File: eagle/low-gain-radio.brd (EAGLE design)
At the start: 99 x 98 mm, 131 parts, among them U1 MKW01Z128, U2 SKY65116, U3 W25Q80DV, U4 LP5907MFX-3.3, U6 LP5907MFX-3.3, U7 LD39200, U8 MAAL-010704, Y1 32MHz

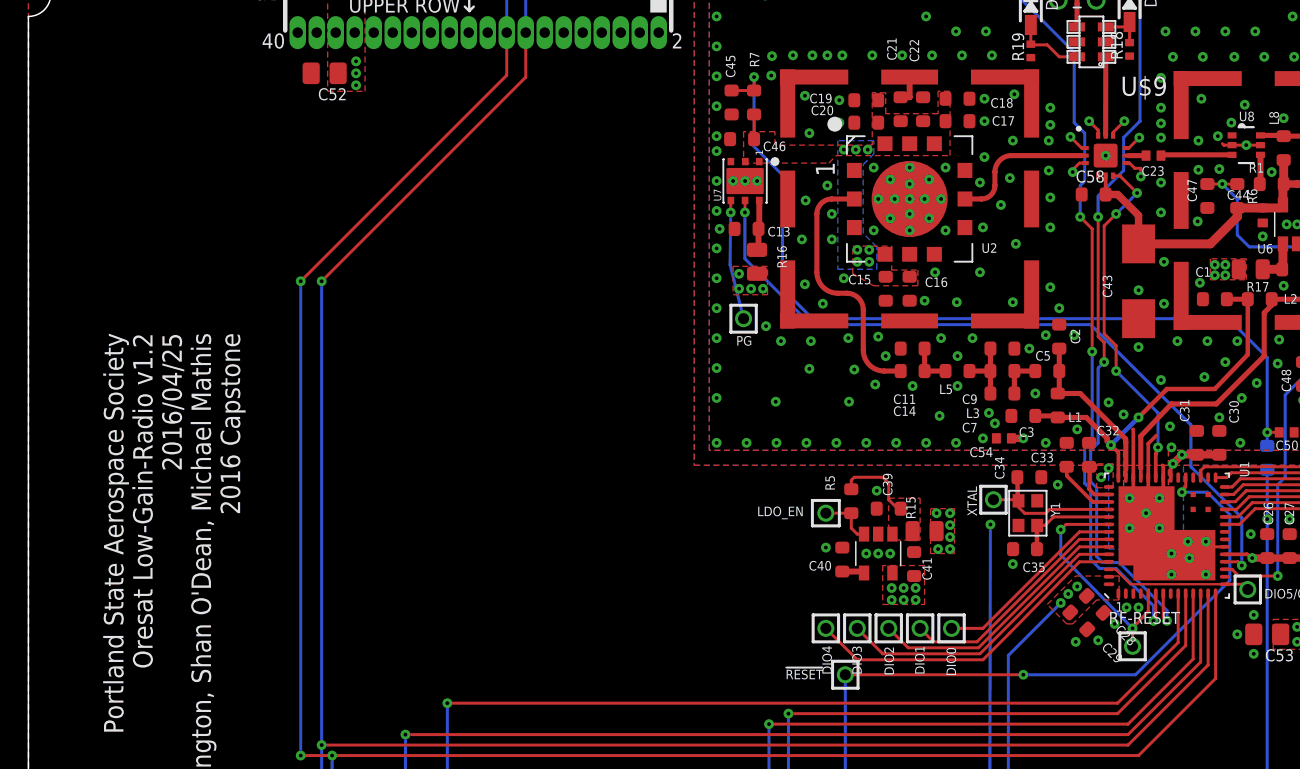
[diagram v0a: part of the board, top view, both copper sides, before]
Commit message: small tweaks on layout, including more gnd vias
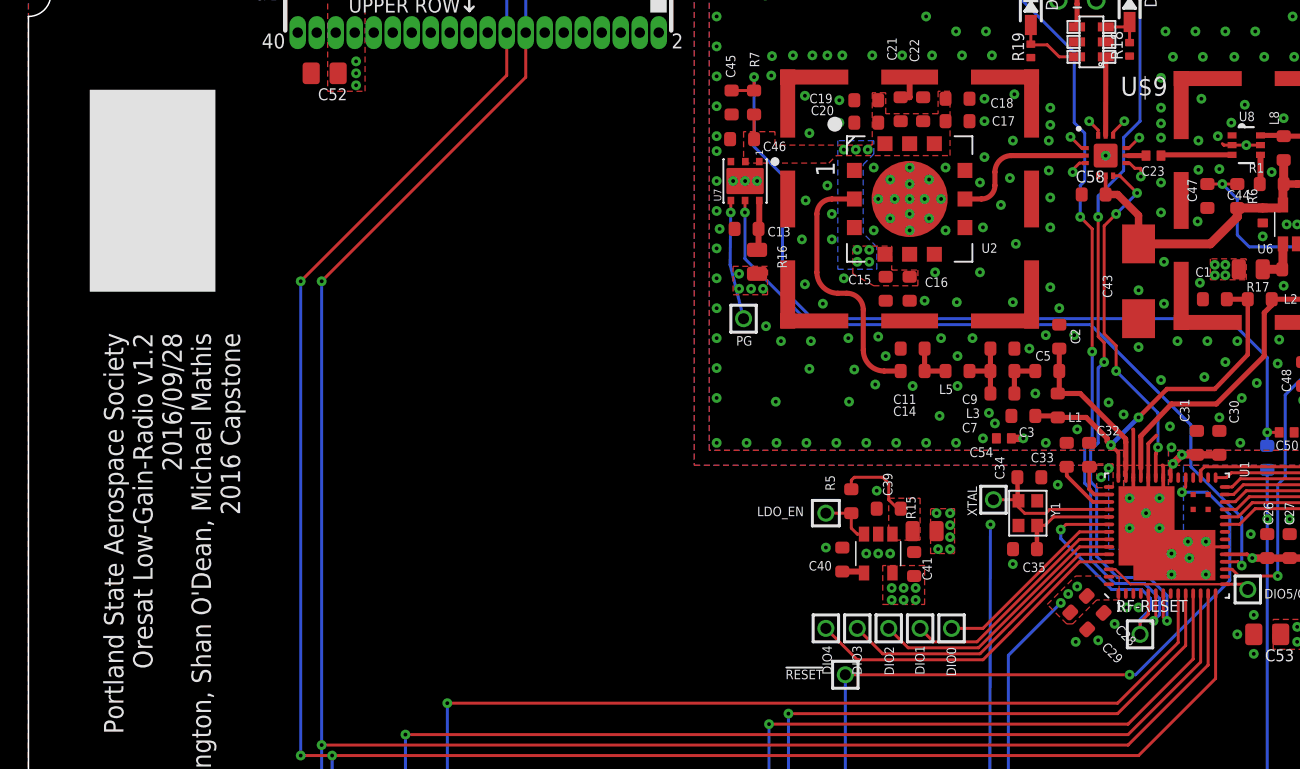
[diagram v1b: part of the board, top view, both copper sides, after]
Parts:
- moved RF-RESET 0.94 mm to (74.3, 48.7)
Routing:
- net RF_RESET: track 15.9 -> 17.3 mm, vias 2 -> 1
- net VFWD: track 51.9 -> 52.7 mm
- net VREV: track 51.6 -> 52.2 mm
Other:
- board text added: "Portland State Aerospace Society Oresat Low-Gain-Radio v1.2 2016/09/28 James Heath, Will Harrington, Shan O'Dean, Michael Mathis 2016 Capstone"
- board text removed: "Portland State Aerospace Society Oresat Low-Gain-Radio v1.2 2016/04/25 James Heath, Will Harrington, Shan O'Dean, Michael Mathis 2016 Capstone"
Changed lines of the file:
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@@
 <text x="5.05" y="68.85" size="1.3" layer="21" font="vector" ratio="15" rot="R270">Portland State Aerospace Society
 Oresat Low-Gain-Radio v1.2
-2016/04/25
+2016/09/28
 James Heath, Will Harrington, Shan O'Dean, Michael Mathis
 2016 Capstone</text>
@@
 <wire x1="56.3" y1="78.2" x2="56.3" y2="77.3" width="0.1" layer="41"/>
 <wire x1="58.5" y1="80.35" x2="59.3" y2="80.35" width="0.01" layer="41"/>
+<rectangle x1="4.1" y1="71.6" x2="12.5" y2="85.1" layer="21"/>
 </plain>
 <attributes>
@@
 <element name="CF2" library="oresat-eagle" package="CON-MMCX-F-MOLEX-0734151001" value="CON-MMCX-F-MOLEX-0734151001" x="70.1" y="92.35"/>
 <element name="U$35" library="oresat-eagle" package="ORESAT-CARD-RF-V0.4" value="" x="0" y="0"/>
-<element name="RF-RESET" library="Tova" package="2MM-TEST-POINT" value="TEST-POINT" x="73.8" y="47.9"/>
+<element name="RF-RESET" library="Tova" package="2MM-TEST-POINT" value="TEST-POINT" x="74.3" y="48.7"/>
 <element name="C58" library="rcl_custom" package=".0603-B-NOSILK" value="10nF" x="71.2" y="78.1">
 <attribute name="DIST" value="Digi-Key" x="71.2" y="78.1" size="1.778" layer="27" display="off"/>
@@
 <contactref element="CM1" pad="10"/>
 <contactref element="U1" pad="33"/>
-<via x="66.5" y="46" extent="1-16" drill="0.254"/>
+<via x="73.6" y="46" extent="1-16" drill="0.254"/>
 <contactref element="!RESET" pad="1"/>
 <wire x1="77.35" y1="59.1778" x2="77.35" y2="58.55" width="0.2" layer="1"/>
@@
 <wire x1="78.8" y1="58.2" x2="80.3" y2="56.7" width="0.2" layer="16"/>
 <wire x1="80.3" y1="56.7" x2="80.3" y2="52.3" width="0.2" layer="16"/>
-<wire x1="66.5" y1="46" x2="54.6" y2="46" width="0.2" layer="1"/>
+<wire x1="73.6" y1="46" x2="54.6" y2="46" width="0.2" layer="1"/>
 <wire x1="54.6" y1="46" x2="54.6" y2="4.055" width="0.2" layer="16"/>
 <wire x1="54.6" y1="4.055" x2="54.61" y2="4.045" width="0.2" layer="16"/>
 <wire x1="80.3" y1="52.3" x2="74" y2="46" width="0.2" layer="16"/>
-<wire x1="74" y1="46" x2="66.5" y2="46" width="0.2" layer="16"/>
+<wire x1="74" y1="46" x2="73.6" y2="46" width="0.2" layer="16"/>
 </signal>
 <signal name="N$4">
@@
 <wire x1="75.85" y1="49.85" x2="76.1" y2="49.6" width="0.2" layer="1"/>
 <via x="76.1" y="49.6" extent="1-16" drill="0.254"/>
-<wire x1="76.1" y1="49.6" x2="76.1" y2="50.3" width="0.2" layer="16"/>
-<wire x1="76.1" y1="50.3" x2="72.9" y2="53.5" width="0.2" layer="16"/>
-<wire x1="72.9" y1="53.5" x2="71.8" y2="53.5" width="0.2" layer="16"/>
-<wire x1="71.8" y1="53.5" x2="71.4" y2="53.9" width="0.2" layer="16"/>
 <wire x1="71.4" y1="53.9" x2="71.4" y2="58.5" width="0.2" layer="16"/>
 <via x="71.9" y="66.9" extent="1-16" drill="0.254"/>
@@
 <wire x1="75.45" y1="93.5" x2="76.25" y2="93.5" width="0.2" layer="1"/>
 <wire x1="76.25" y1="93.5" x2="76.3" y2="93.45" width="0.2" layer="1"/>
+<wire x1="71.4" y1="53.9" x2="72.8" y2="52.5" width="0.2" layer="16"/>
+<wire x1="72.8" y1="52.5" x2="74.9" y2="52.5" width="0.2" layer="16"/>
+<wire x1="74.9" y1="52.5" x2="76.1" y2="51.3" width="0.2" layer="16"/>
+<wire x1="76.1" y1="51.3" x2="76.1" y2="49.6" width="0.2" layer="16"/>
 </signal>
 <signal name="FWD">
@@
 <wire x1="75.35" y1="49.75" x2="75.2" y2="49.6" width="0.2" layer="1"/>
 <via x="75.2" y="49.6" extent="1-16" drill="0.254"/>
-<wire x1="75.2" y1="49.6" x2="75.2" y2="50.6" width="0.2" layer="16"/>
-<wire x1="75.2" y1="50.6" x2="72.7" y2="53.1" width="0.2" layer="16"/>
-<wire x1="72.7" y1="53.1" x2="71.6" y2="53.1" width="0.2" layer="16"/>
-<wire x1="71.6" y1="53.1" x2="71" y2="53.7" width="0.2" layer="16"/>
 <wire x1="71" y1="53.7" x2="71" y2="58.4" width="0.2" layer="16"/>
 <via x="71.1" y="67.6" extent="1-16" drill="0.254"/>
@@
 <wire x1="65.25" y1="93.3" x2="64.45" y2="93.3" width="0.2" layer="1"/>
 <wire x1="64.45" y1="93.3" x2="64.4" y2="93.25" width="0.2" layer="1"/>
+<wire x1="71" y1="53.7" x2="72.6" y2="52.1" width="0.2" layer="16"/>
+<wire x1="72.6" y1="52.1" x2="74.6" y2="52.1" width="0.2" layer="16"/>
+<wire x1="74.6" y1="52.1" x2="75.6" y2="51.1" width="0.2" layer="16"/>
+<wire x1="75.2" y1="49.6" x2="75.6" y2="50" width="0.2" layer="16"/>
+<wire x1="75.6" y1="50" x2="75.6" y2="51.1" width="0.2" layer="16"/>
 </signal>
 <signal name="RF_RESET">
 <contactref element="U1" pad="5"/>
 <contactref element="U1" pad="48"/>
-<wire x1="74.85" y1="51.4222" x2="74.85" y2="50.25" width="0.2" layer="1"/>
-<wire x1="74.85" y1="50.25" x2="73.8" y2="49.1" width="0.2" layer="1"/>
-<via x="73.8" y="49.1" extent="1-16" drill="0.254"/>
-<wire x1="73.8" y1="49.1" x2="69" y2="54" width="0.2" layer="16"/>
-<wire x1="69" y1="54" x2="69" y2="55.7" width="0.2" layer="16"/>
+<wire x1="74.85" y1="51.4222" x2="74.85" y2="50.05" width="0.2" layer="1"/>
 <via x="69" y="55.7" extent="1-16" drill="0.254"/>
+<wire x1="69" y1="55.1" x2="69" y2="55.7" width="0.2" layer="16"/>
 <wire x1="69" y1="55.7" x2="69.35" y2="56.05" width="0.2" layer="1"/>
 <wire x1="72.2222" y1="56.05" x2="69.35" y2="56.05" width="0.2" layer="1"/>
 <contactref element="RF-RESET" pad="1"/>
-<wire x1="73.8" y1="47.9" x2="73.8" y2="49.1" width="0.2" layer="1"/>
+<wire x1="74.85" y1="50.05" x2="74.3" y2="49.5" width="0.2" layer="1"/>
+<wire x1="74.3" y1="49.5" x2="74.3" y2="48.7" width="0.2" layer="1"/>
+<wire x1="74.3" y1="48.7" x2="74.3" y2="49.7" width="0.2" layer="16"/>
+<wire x1="74.3" y1="49.7" x2="75" y2="50.4" width="0.2" layer="16"/>
+<wire x1="75" y1="50.4" x2="75" y2="51.1" width="0.2" layer="16"/>
+<wire x1="75" y1="51.1" x2="74.4" y2="51.7" width="0.2" layer="16"/>
+<wire x1="74.4" y1="51.7" x2="72.4" y2="51.7" width="0.2" layer="16"/>
+<wire x1="72.4" y1="51.7" x2="69" y2="55.1" width="0.2" layer="16"/>
 </signal>
 <signal name="N$12">

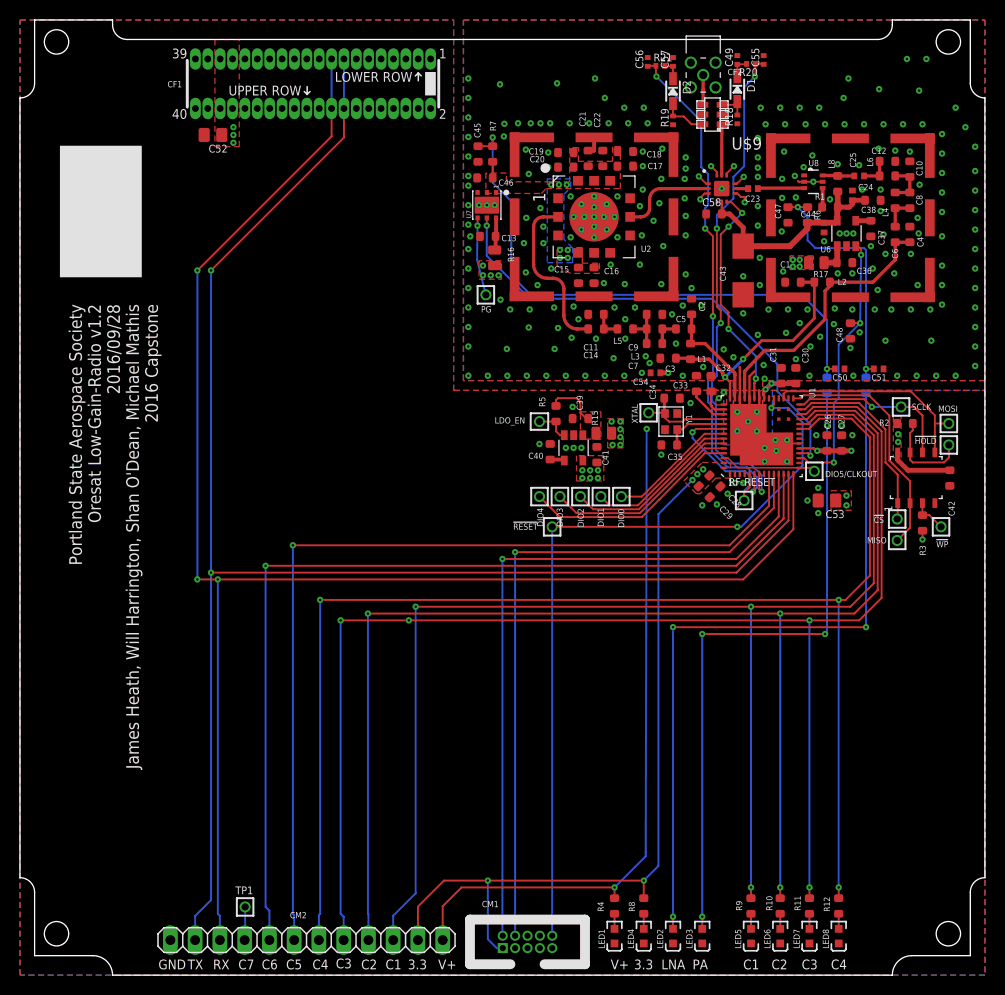
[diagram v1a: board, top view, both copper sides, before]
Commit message: added new RF switch, started layout but its unfinished, still need to hook GPIO to 40 pin connector as well
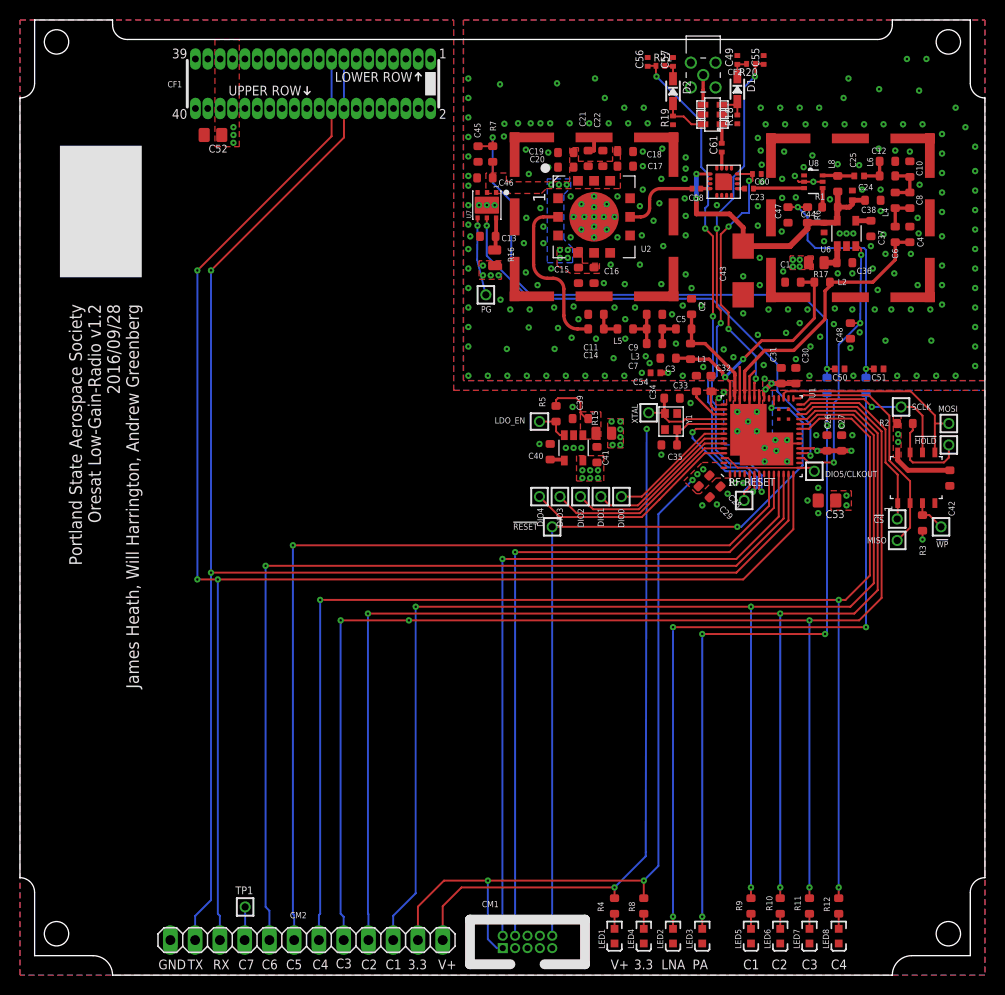
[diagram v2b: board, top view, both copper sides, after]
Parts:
- removed U$9: PE42723, low-gain-radio:PE42723
- added C60, C61: 100pF, low-gain-radio:.0402-C-NOSILK
- added U$49: RF3025, low-gain-radio:QFN-16_3MMX3MM
- C23: value 1nF -> 100pF; device rcl_custom:.0402-B-NOSILK -> low-gain-radio:.0402-C-NOSILK
- C58: value 10nF -> 100pF; device rcl_custom:.0603-B-NOSILK -> low-gain-radio:.0402-C-NOSILK
- moved C58 3.16 mm to (69.4, 80.7)
- moved C23 0.40 mm to (74.8, 80.7), turned to 180 degrees
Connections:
- new net RFOUT: C58.1, U2.8
- new net RXTX_OUT: C61.1, U$49.RFC
- net LNA_IN: now also C23.2, U$49.RF2; no longer C23.1, U$9.8
- net N$25: now also C23.1; no longer C23.2
- net PA_IN: now also C58.2, U$49.RF1; no longer U$9.2, U2.8
- net RFC: now also C61.2; no longer U$9.11
- net RF_GND: now also C60.1, U$49.GND, U$49.GND1, U$49.GND10, U$49.GND2, U$49.GND3, U$49.GND4, U$49.GND5, U$49.GND6, U$49.GND7, U$49.GND8, U$49.GND9, U$49.PADDLE; no longer C58.1, U$9.1, U$9.10, U$9.12, U$9.3, U$9.7, U$9.9
- net RXTX: now also C60.2, U$49.VC; no longer U$9.6
- net VBIAS: now also U$49.VDD; no longer C58.2, U$9.5
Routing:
- net PA_IN: track 9.78 -> 0.95 mm
- net RFOUT: track 0.00 -> 8.08 mm
- net RF_GND: track 26.1 -> 18.3 mm, vias 253 -> 247
- net VBIAS: track 23.5 -> 30.3 mm, vias 0 -> 2
- net RXTX: track 23.5 -> 28.0 mm
- net RFC: track 5.25 -> 1.96 mm
- net RXTX_OUT: track 0.00 -> 1.65 mm
- net LNA_IN: track 1.35 -> 0.75 mm
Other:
- board text added: "Portland State Aerospace Society Oresat Low-Gain-Radio v1.2 2016/09/28 James Heath, Will Harrington, Andrew Greenberg"
- board text removed: "Portland State Aerospace Society Oresat Low-Gain-Radio v1.2 2016/09/28 James Heath, Will Harrington, Shan O'Dean, Michael Mathis 2016 Capstone"

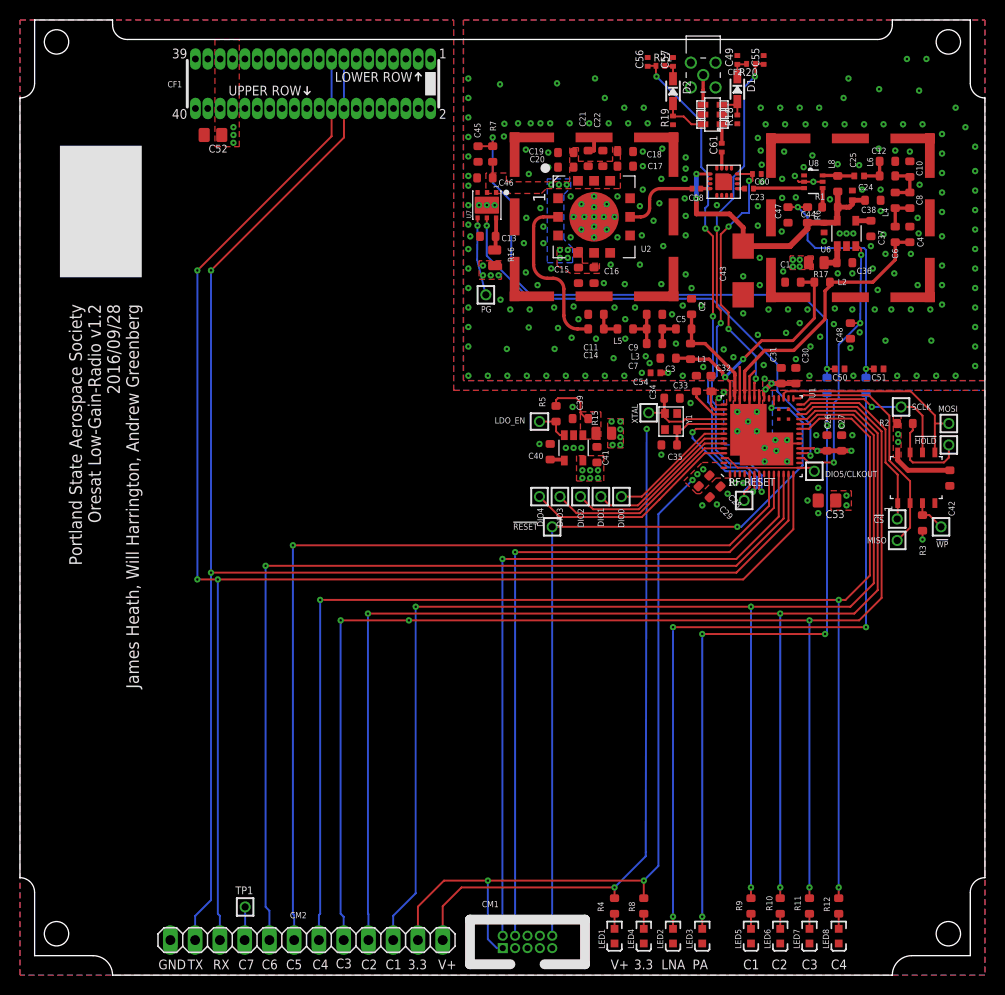
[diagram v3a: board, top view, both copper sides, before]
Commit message: finished with laying out the rf switch, placed and routed GPIO line for LLWU
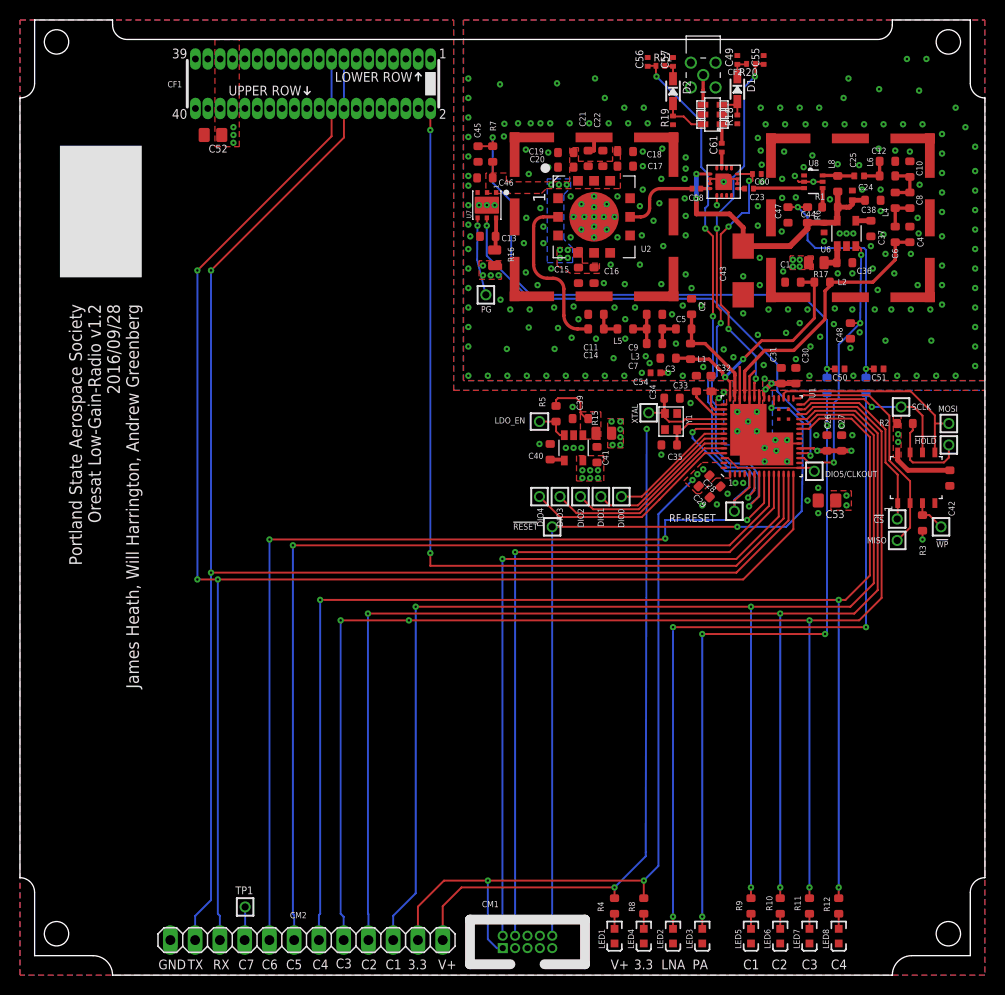
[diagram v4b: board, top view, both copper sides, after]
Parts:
- moved RF-RESET 1.49 mm to (73.3, 47.6)
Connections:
- removed net PTA4: CM2.8, U1.12
- new net PTA4/NMI_B: CF1.P$2, U1.12
- new net PTE19: CM2.8, U1.8
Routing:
- net PTA4: track 98.3 -> 0.00 mm, vias 1 -> 0
- net PTE19: track 0.00 -> 97.5 mm, vias 0 -> 3
- net PTA4/NMI_B: track 0.00 -> 89.8 mm, vias 0 -> 2
- net RF_GND: track 18.3 -> 23.4 mm, vias 247 -> 248
- net VREV: track 52.2 -> 55.8 mm
- net RF_RESET: track 17.3 -> 20.2 mm
- net !RESET: track 79.6 -> 82.3 mm
- net VFWD: track 52.7 -> 54.0 mm
